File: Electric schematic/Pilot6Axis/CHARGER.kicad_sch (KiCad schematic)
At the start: 10 parts, among them J17 TP4056, J18 BAT

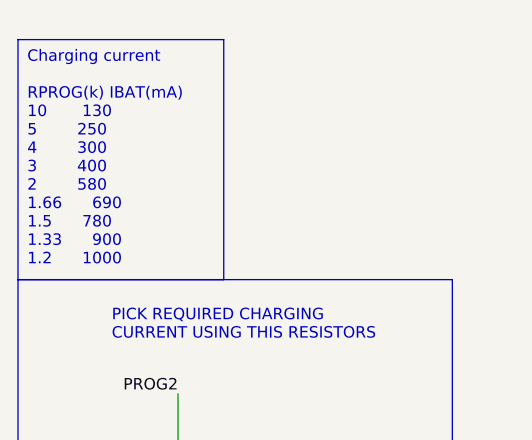
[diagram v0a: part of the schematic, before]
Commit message: update schematic to kicajd 9.0,    fixed usb D=/D- wrongly inerconnected , otherwise pcb seems to be woekring
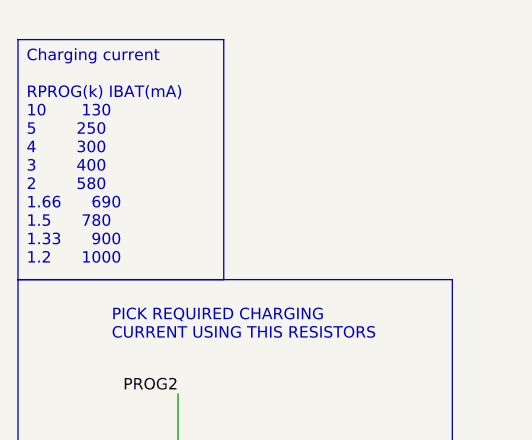
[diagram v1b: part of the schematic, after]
